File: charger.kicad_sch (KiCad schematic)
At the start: 0 parts

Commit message: Add gauge schematic and partial charger schematic
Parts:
- added C5 (x3): 150pF, Capacitor_SMD:C_0402_1005Metric, symbol Device:C_Small
- added C5: 33pF, Capacitor_SMD:C_0402_1005Metric, symbol Device:C_Small
- added C5: 2.2nF, Capacitor_SMD:C_0402_1005Metric, symbol Device:C_Small
- added C5: 10nF, Capacitor_SMD:C_0402_1005Metric, symbol Device:C_Small
- added C5: 680pF, Capacitor_SMD:C_0603_1608Metric, symbol Device:C_Small
- added C5 (x2): 100nF, Capacitor_SMD:C_0402_1005Metric, symbol Device:C_Small
- added C5: 15pF, Capacitor_SMD:C_0402_1005Metric, symbol Device:C_Small
- added C5: 2.2uF, Capacitor_SMD:C_0603_1608Metric, symbol Device:C_Small
- added C5 (x2): 1uF, Capacitor_SMD:C_0402_1005Metric, symbol Device:C_Small
- added L3: 2.2uH, Inductor_SMD:L_Taiyo-Yuden_MD-4040, symbol Device:L_Small
- added Q4, Q5, Q6, Q7, Q8: CSD17308Q3, Package_DFN_FET:DFN-8-FET_3x3mm_P0.65mm, symbol Transistor_FET_DFN:AON7544
- added R12: 33k, Resistor_SMD:R_0402_1005Metric, symbol Device:R_Small
- added R12: 27k, Resistor_SMD:R_0402_1005Metric, symbol Device:R_Small
- added R12 (x2): 100k, Resistor_SMD:R_0402_1005Metric, symbol Device:R_Small
- added R12: 10k, Resistor_SMD:R_0402_1005Metric, symbol Device:R_Small
- added R12: 10R, Resistor_SMD:R_0402_1005Metric, symbol Device:R_Small
- added R12: 150k, Resistor_SMD:R_0402_1005Metric, symbol Device:R_Small
- added U8: BQ25703A, Package_DFN_QFN:QFN-32-1EP_4x4mm_P0.4mm_EP2.65x2.65mm, symbol ti-chargers:BQ25703A
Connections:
- new net: C5.2, Q4.4 (G), U8.29 (LODRV1)
- new net: C5.1, R12.1 (x2)
- new net: C5.2, C5.2, U8.16 (COMP1)
- new net: C5.2, R12.1, R12.2, U8.6 (ILIM_HIZ)
- new net: C5.1, Q7.5 (D), Q7.6 (D), Q7.7 (D), Q7.8 (D), Q7.9 (D)
- new net: C5.2, C5.2, U8.17 (COMP2)
- new net: C5.1, L3.1, Q4.5 (D), Q4.6 (D), Q4.7 (D), Q4.8 (D), Q4.9 (D), Q7.1 (S), Q7.2 (S), Q7.3 (S), U8.32 (SW1)
- new net: C5.2, U8.30 (BTST1)
- new net: R12.1, R12.1, U8.18 (CELL_BATPRESZ)
- new net: C5.2, Q5.4 (G), U8.26 (LODRV2)
- new net: Q8.4 (G), U8.21 (~{BATDRV})
- new net: Q6.5 (D), Q6.6 (D), Q6.7 (D), Q6.8 (D), Q6.9 (D), Q8.5 (D), Q8.6 (D), Q8.7 (D), Q8.8 (D), Q8.9 (D), U8.22 (VSYS)
- new net: C5.1, L3.2, Q5.5 (D), Q5.6 (D), Q5.7 (D), Q5.8 (D), Q5.9 (D), Q6.1 (S), Q6.2 (S), Q6.3 (S), U8.23 (SW2)
- new net: Q6.4 (G), U8.24 (HIDRV2)
- new net: C5.2, U8.25 (BTST2)
- new net: C5.2, R12.2, U8.28 (REGN)
- new net: Q7.4 (G), U8.31 (HIDRV1)
- new net: C5.1, R12.1, R12.1, R12.2, U8.7 (VDDA)
- new net: C5.1, Q8.1 (S), Q8.2 (S), Q8.3 (S)
- new net GND: C5.1, C5.1, C5.1, C5.1, C5.1, C5.1, C5.2, C5.2, C5.2, Q4.1 (S), Q4.2 (S), Q4.3 (S), Q5.1 (S), Q5.2 (S), Q5.3 (S), R12.2, R12.2, R12.2, R12.2, U8.27 (PGND), U8.33 (PGND)
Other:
- note added: "2S"

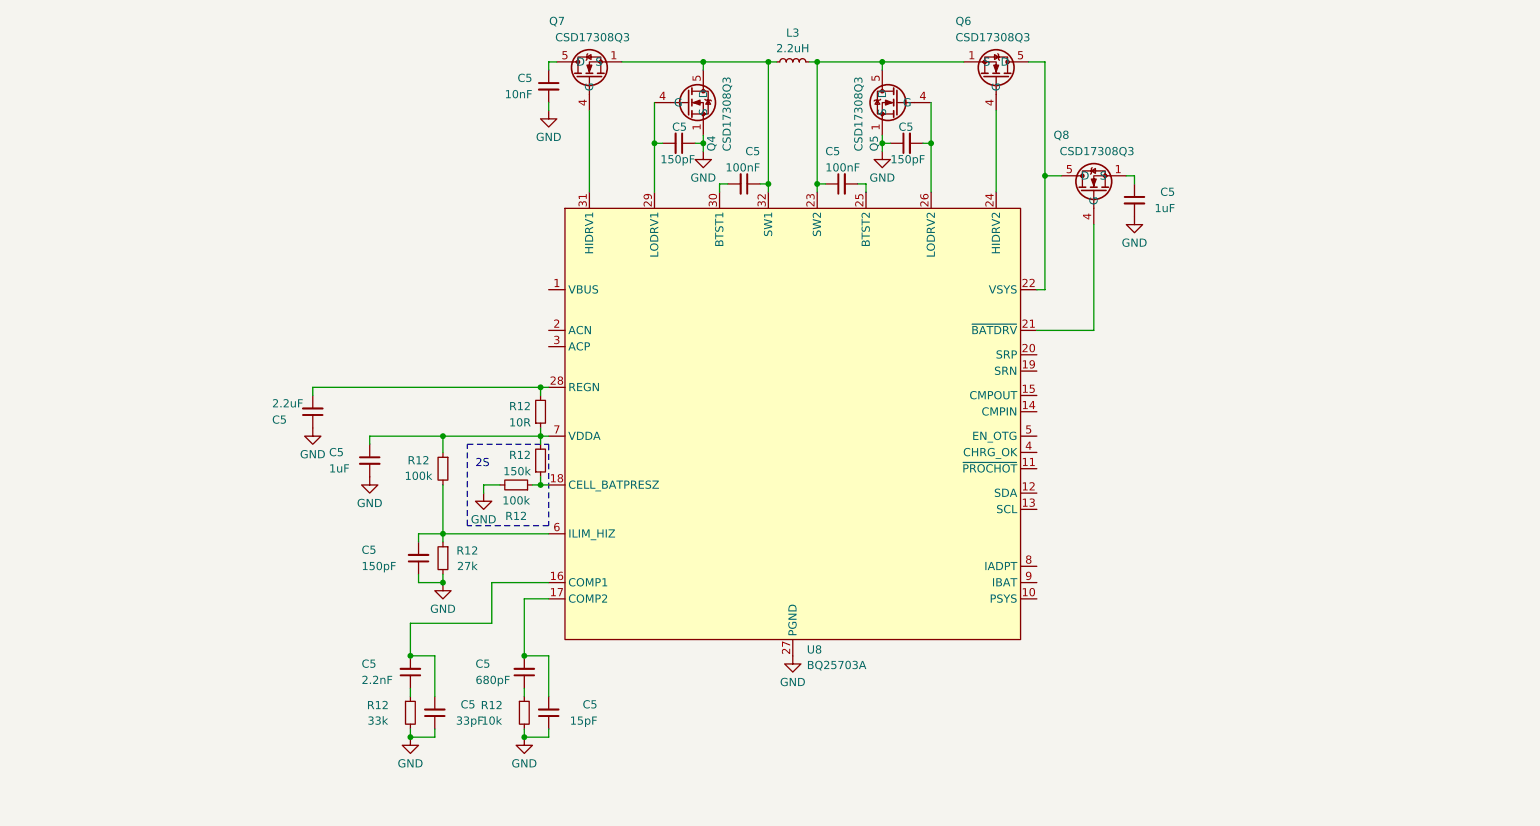
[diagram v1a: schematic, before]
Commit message: Finish preliminary charger and logic schematic
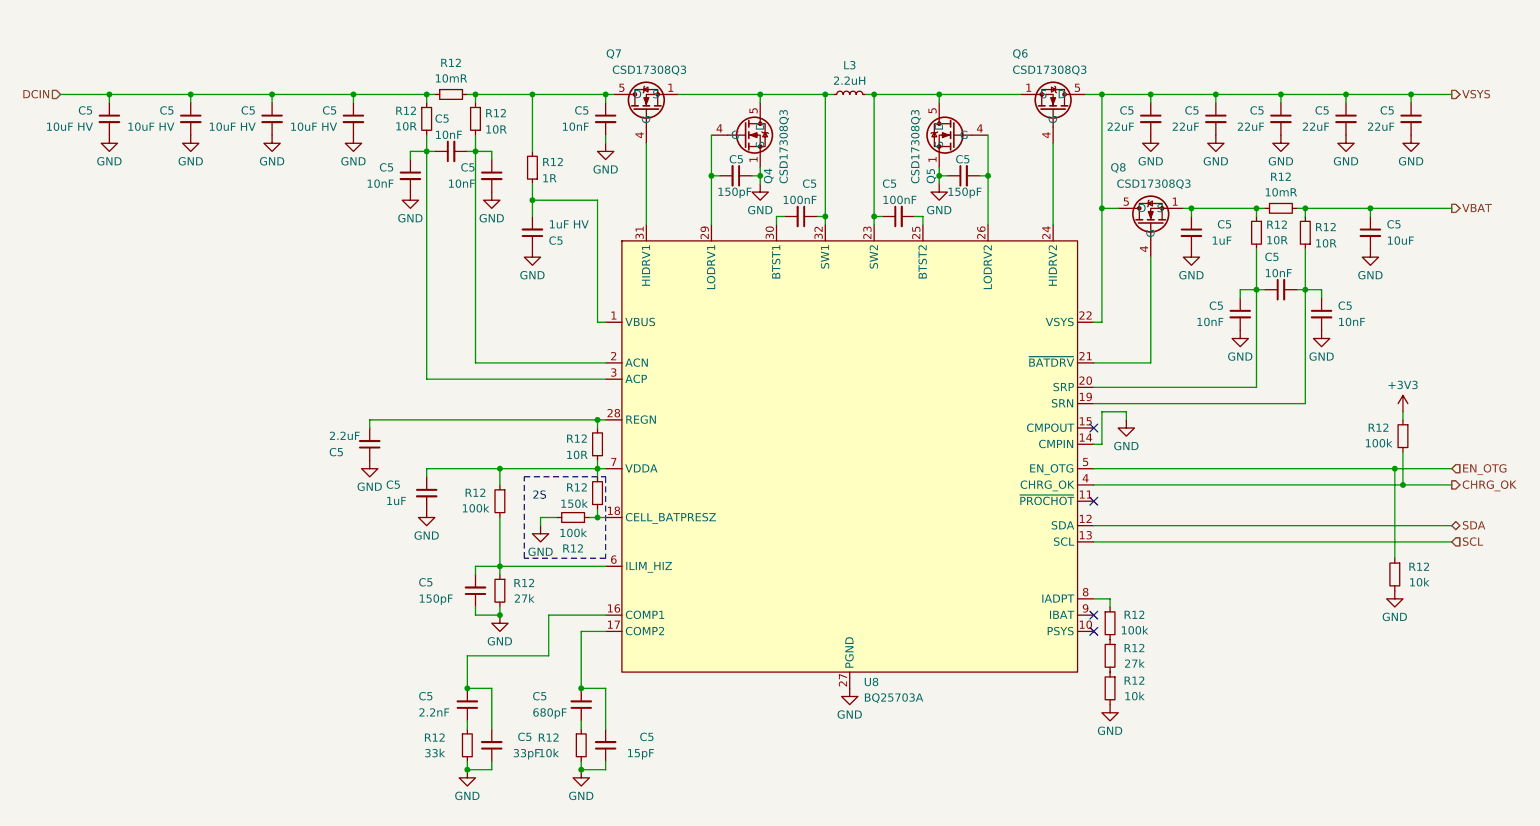
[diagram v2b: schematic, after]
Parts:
- added C5 (x5): 22uF, Capacitor_SMD:C_0805_2012Metric, symbol Device:C_Small
- added C5 (x4): 10uF HV, Capacitor_SMD:C_0805_2012Metric, symbol Device:C_Small
- added C5 (x6): 10nF, Capacitor_SMD:C_0402_1005Metric, symbol Device:C_Small
- added C5: 1uF HV, Capacitor_SMD:C_0603_1608Metric, symbol Device:C_Small
- added C5: 10uF, Capacitor_SMD:C_0805_2012Metric, symbol Device:C_Small
- added R12 (x4): 10R, Resistor_SMD:R_0402_1005Metric, symbol Device:R_Small
- added R12 (x2): 10k, Resistor_SMD:R_0402_1005Metric, symbol Device:R_Small
- added R12 (x2): 10mR, Resistor_SMD:R_0805_2012Metric, symbol Device:R_Small
- added R12: 1R, Resistor_SMD:R_0402_1005Metric, symbol Device:R_Small
- added R12 (x2): 100k, Resistor_SMD:R_0402_1005Metric, symbol Device:R_Small
- added R12: 27k, Resistor_SMD:R_0402_1005Metric, symbol Device:R_Small
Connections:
- net GND: now also U8.14 (CMPIN), C5.1, C5.2, C5.2, C5.2, C5.2, C5.2, C5.2, C5.2, C5.2, C5.2, C5.2, C5.2, C5.2, C5.2, C5.2, R12.2, R12.2
- net at C5.1, Q7.5 (D), Q7.6 (D)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: now also R12.2, R12.2, R12.2
- net at U8.1 (VBUS): now also C5.2, R12.1
- net SDA: now reaches U8.12 (SDA)
- net SCL: now reaches U8.13 (SCL)
- net at U8.19 (SRN): now also C5.1, C5.2, R12.1
- net at U8.2 (ACN): now also C5.1, C5.2, R12.1
- net at U8.20 (SRP): now also C5.1, C5.1, R12.2
- net VSYS: now reaches Q6.5 (D), Q6.6 (D), Q6.7 (D), Q6.8 (D), Q6.9 (D), Q8.5 (D), Q8.6 (D), Q8.7 (D), Q8.8 (D), Q8.9 (D), U8.22 (VSYS)
- net VSYS: now also C5.1, C5.1, C5.1, C5.1, C5.1
- net at U8.3 (ACP): now also C5.1, C5.1, R12.2
- net CHRG_OK: now reaches U8.4 (CHRG_OK)
- net CHRG_OK: now also R12.2
- net EN_OTG: now reaches U8.5 (EN_OTG)
- net EN_OTG: now also R12.1
- net at U8.8 (IADPT): now also R12.1
- net at C5.1, Q8.1 (S), Q8.2 (S)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: now also R12.1, R12.1
- new net: R12.1, R12.2 (x2)
- new net +3V3: R12.1
- new net DCIN: C5.1, C5.1, C5.1, C5.1, R12.1, R12.1
- new net VBAT: C5.1, R12.2, R12.2
- no-connect marks 0 -> 4
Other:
- moved on the sheet: C5, L3, Q4, Q5, Q6, Q7, Q8, R12, U8

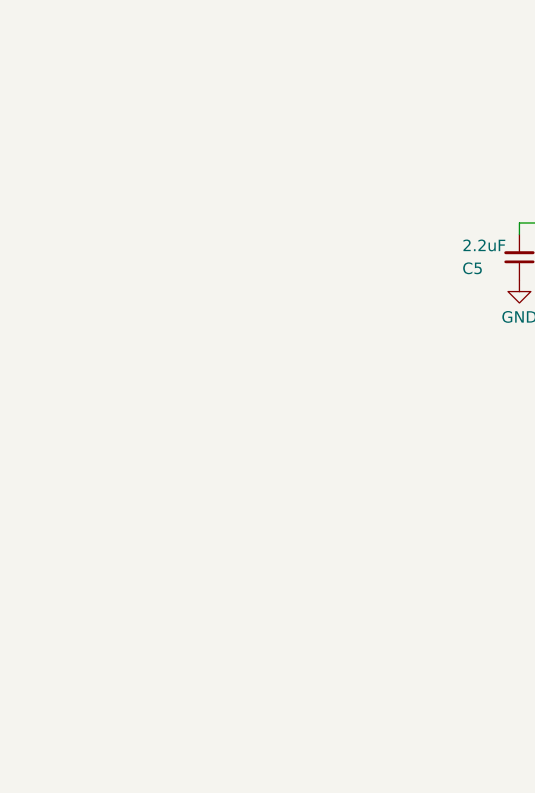
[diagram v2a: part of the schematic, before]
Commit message: Add list of 1S charger chips
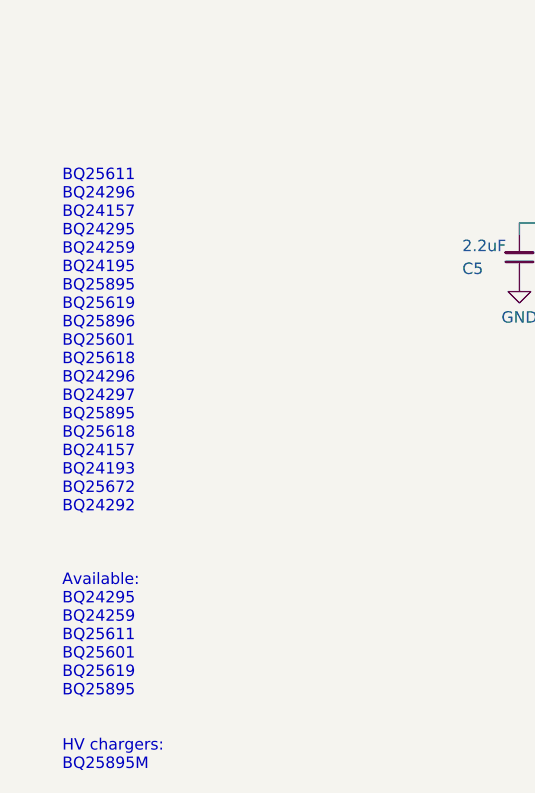
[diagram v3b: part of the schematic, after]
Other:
- note added: "BQ25611 BQ24296 BQ24157 BQ24295 BQ24259 BQ24195 BQ25895 BQ25619 BQ25896 BQ25601 BQ25618 BQ24296 BQ24297 BQ25895 BQ25618 BQ24157 BQ24193 BQ25672 BQ24292 Available: BQ24295 BQ24259 BQ25611 BQ25601 BQ25619 BQ25895 HV chargers: BQ25895M"
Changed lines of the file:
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@@
     (fill (type none))
+  )
+  (text "BQ25611\nBQ24296\nBQ24157\nBQ24295\nBQ24259\nBQ24195\nBQ25895\nBQ25619\nBQ25896\nBQ25601\nBQ25618\nBQ24296\nBQ24297\nBQ25895\nBQ25618\nBQ24157\nBQ24193\nBQ25672\nBQ24292\n\n\n\nAvailable:\nBQ24295\nBQ24259\nBQ25611\nBQ25601\nBQ25619\nBQ25895\n\n\nHV chargers:\nBQ25895M\n"
+    (at 21.59 156.21 0)
+    (effects (font (size 1.27 1.27)) (justify left bottom))
   )
   (text "2S" (at 97.79 107.95 0)

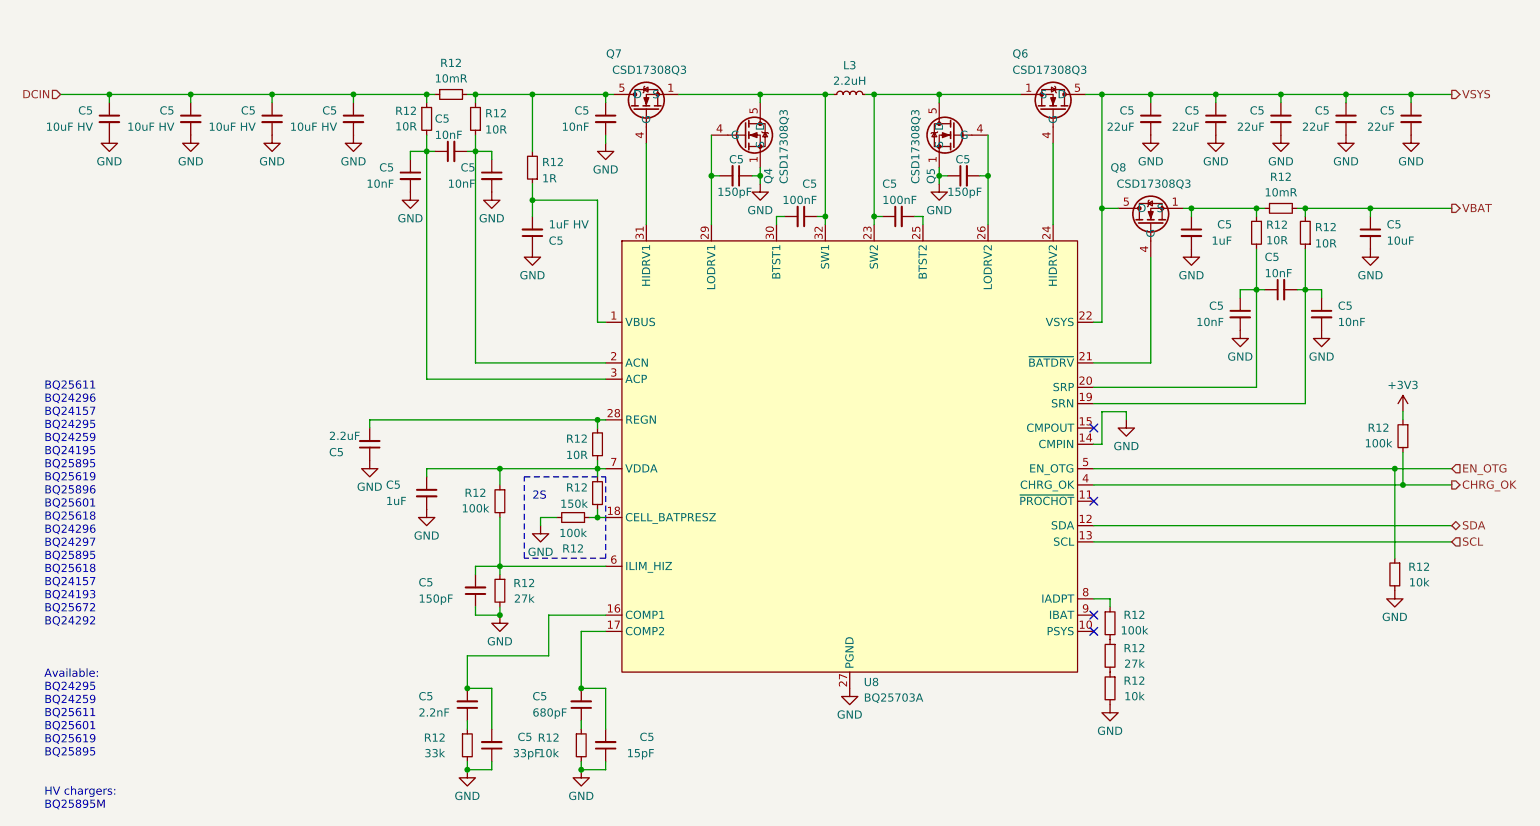
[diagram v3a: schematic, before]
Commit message: Finish rough layout
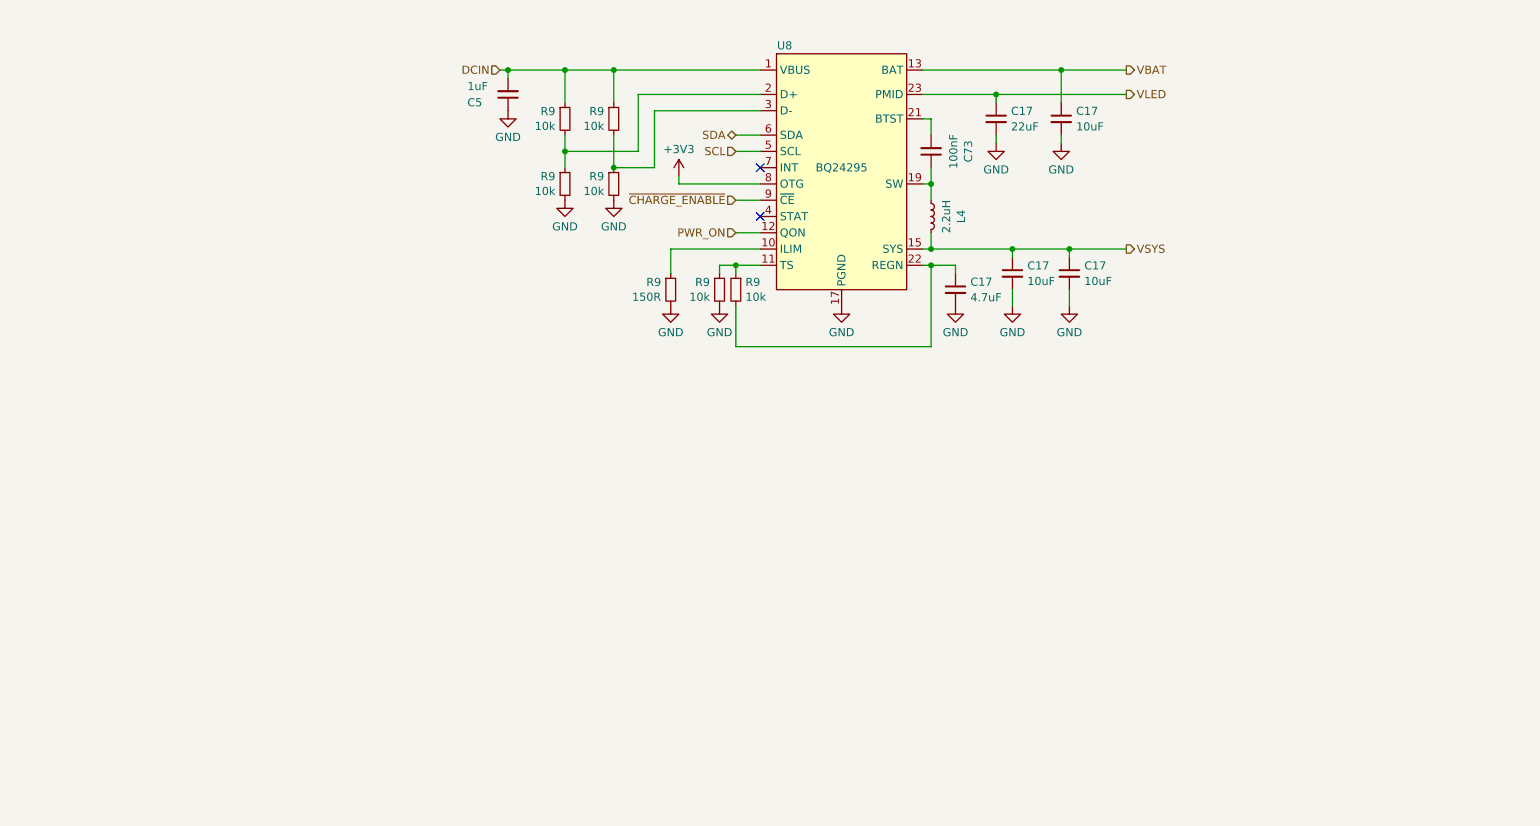
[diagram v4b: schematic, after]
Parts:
- removed C5 (x5): 22uF, Capacitor_SMD:C_0805_2012Metric, symbol Device:C_Small
- removed C5 (x3): 150pF, Capacitor_SMD:C_0402_1005Metric, symbol Device:C_Small
- removed C5: 33pF, Capacitor_SMD:C_0402_1005Metric, symbol Device:C_Small
- removed C5: 2.2nF, Capacitor_SMD:C_0402_1005Metric, symbol Device:C_Small
- removed C5 (x4): 10uF HV, Capacitor_SMD:C_0805_2012Metric, symbol Device:C_Small
- removed C5 (x7): 10nF, Capacitor_SMD:C_0402_1005Metric, symbol Device:C_Small
- removed C5: 680pF, Capacitor_SMD:C_0603_1608Metric, symbol Device:C_Small
- removed C5 (x2): 100nF, Capacitor_SMD:C_0402_1005Metric, symbol Device:C_Small
- removed C5: 1uF HV, Capacitor_SMD:C_0603_1608Metric, symbol Device:C_Small
- removed C5: 15pF, Capacitor_SMD:C_0402_1005Metric, symbol Device:C_Small
- removed C5: 10uF, Capacitor_SMD:C_0805_2012Metric, symbol Device:C_Small
- removed C5: 2.2uF, Capacitor_SMD:C_0603_1608Metric, symbol Device:C_Small
- removed C5 (x2): 1uF, Capacitor_SMD:C_0402_1005Metric, symbol Device:C_Small
- removed L3: 2.2uH, Inductor_SMD:L_Taiyo-Yuden_MD-4040, symbol Device:L_Small
- removed Q4, Q5, Q6, Q7, Q8: CSD17308Q3, Package_DFN_FET:DFN-8-FET_3x3mm_P0.65mm, symbol Transistor_FET_DFN:AON7544
- removed R12 (x5): 10R, Resistor_SMD:R_0402_1005Metric, symbol Device:R_Small
- removed R12 (x3): 10k, Resistor_SMD:R_0402_1005Metric, symbol Device:R_Small
- removed R12 (x2): 10mR, Resistor_SMD:R_0805_2012Metric, symbol Device:R_Small
- removed R12: 33k, Resistor_SMD:R_0402_1005Metric, symbol Device:R_Small
- removed R12 (x2): 27k, Resistor_SMD:R_0402_1005Metric, symbol Device:R_Small
- removed R12 (x4): 100k, Resistor_SMD:R_0402_1005Metric, symbol Device:R_Small
- removed R12: 1R, Resistor_SMD:R_0402_1005Metric, symbol Device:R_Small
- removed R12: 150k, Resistor_SMD:R_0402_1005Metric, symbol Device:R_Small
- removed U8: BQ25703A, Package_DFN_QFN:QFN-32-1EP_4x4mm_P0.4mm_EP2.65x2.65mm, symbol ti-chargers:BQ25703A
- added C17 (x3): 10uF, Capacitor_SMD:C_0603_1608Metric, symbol Device:C_Small
- added C17: 22uF, Capacitor_SMD:C_0805_2012Metric, symbol Device:C_Small
- added C17: 4.7uF, Capacitor_SMD:C_0402_1005Metric, symbol Device:C_Small
- added C5: 1uF, Capacitor_SMD:C_0402_1005Metric, symbol Device:C_Small
- added C73: 100nF, Capacitor_SMD:C_0402_1005Metric, symbol Device:C_Small
- added L4: 2.2uH, Inductor_SMD:L_Taiyo-Yuden_MD-4040, symbol Device:L_Small
- added R9 (x6): 10k, Resistor_SMD:R_0402_1005Metric, symbol Device:R_Small
- added R9: 150R, Resistor_SMD:R_0402_1005Metric, symbol Device:R_Small
- added U8: BQ24295, Package_DFN_QFN:QFN-24-1EP_4x4mm_P0.5mm_EP2.7x2.7mm, symbol ti-chargers:BQ24295
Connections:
- net +3V3: now also U8.8 (OTG)
- net GND: now also C17.2, C17.2, C17.2, C17.2, C17.2, C5.1, R9.2, R9.2, R9.2, R9.2, U8.17 (PGND), U8.18 (PGND), U8.25 (PGND)
- net SCL: now also U8.5 (SCL)
- net SDA: now also U8.6 (SDA)
- net VBAT: now also C17.1, U8.13 (BAT), U8.14 (BAT)
- net VSYS: now also C17.1, C17.1, L4.2, U8.15 (SYS), U8.16 (SYS)
- new net: R9.1, U8.10 (ILIM)
- new net: R9.1, R9.1, U8.11 (TS)
- new net: C73.1, L4.1, U8.19 (SW), U8.20 (SW)
- new net: R9.1, R9.2, U8.2 (D+)
- new net: C73.2, U8.21 (BTST)
- new net: C17.1, R9.2, U8.22 (REGN)
- new net: R9.1, R9.2, U8.3 (D-)
- new net PWR_ON: U8.12 (QON)
- new net VBUS: C5.2, R9.1, R9.1, U8.1 (VBUS), U8.24 (VBUS)
- new net VLED: C17.1, U8.23 (PMID)
- new net ~{CHARGE_ENABLE}: U8.9 (~{CE})
- no-connect marks 4 -> 2
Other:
- note removed: "2S"
- note removed: "BQ25611 BQ24296 BQ24157 BQ24295 BQ24259 BQ24195 BQ25895 BQ25619 BQ25896 BQ25601 BQ25618 BQ24296 BQ24297 BQ25895 BQ25618 BQ24157 BQ24193 BQ25672 BQ24292 Available: BQ24295 BQ24259 BQ25611 BQ25601 BQ25619 BQ25895 HV chargers: BQ25895M"

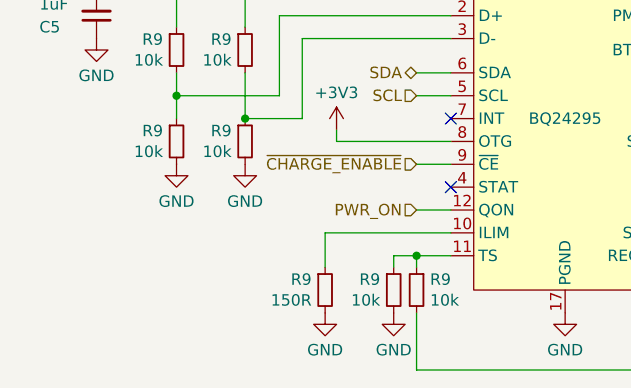
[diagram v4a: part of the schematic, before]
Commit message: Add informational comment on input current limit to schematic
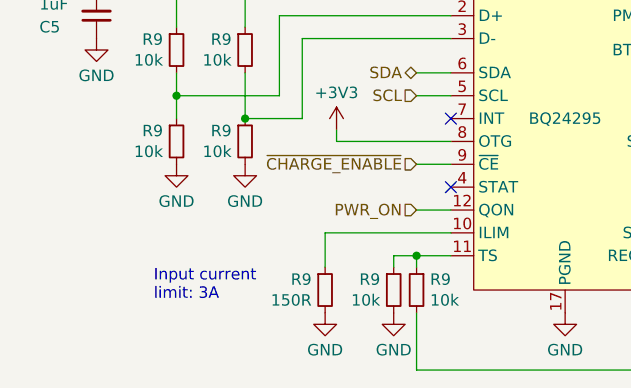
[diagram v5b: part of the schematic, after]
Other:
- note added: "Input current limit: 3A"
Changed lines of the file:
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@@
     (stroke (width 0) (type default))
+  )
+  (text "Input current\nlimit: 3A" (at 100.33 76.2 0)
+    (effects (font (size 1.27 1.27)) (justify left bottom))
   )
   (hierarchical_label "SCL" (shape input) (at 129.54 53.34 180) (fields_autoplaced)
